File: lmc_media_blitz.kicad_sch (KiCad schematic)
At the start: 31 parts, among them J3 Conn_ARM_JTAG_SWD_10, Q1 BSS138, Q2 BSS138, U1 TPS61222DCK, U2 TLV77333PDBVR, U3 LPC804M101JDH20

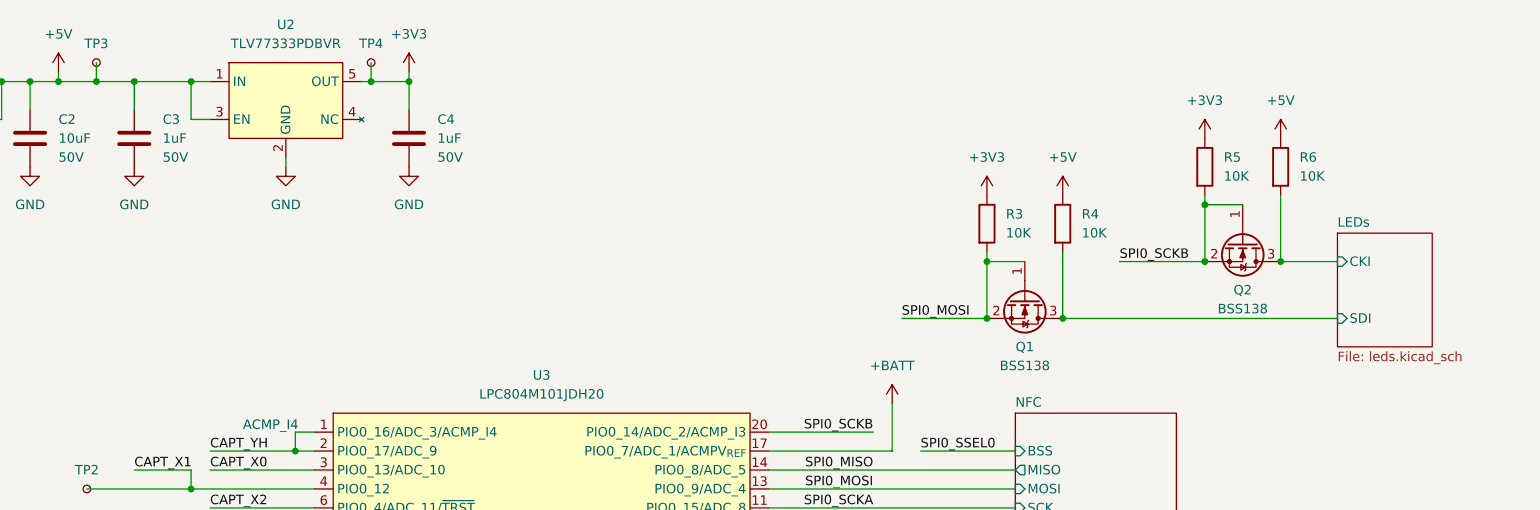
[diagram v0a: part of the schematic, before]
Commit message: Replaced n-channel FETs, LDO, and SWD connector with Basic JLCPCB parts
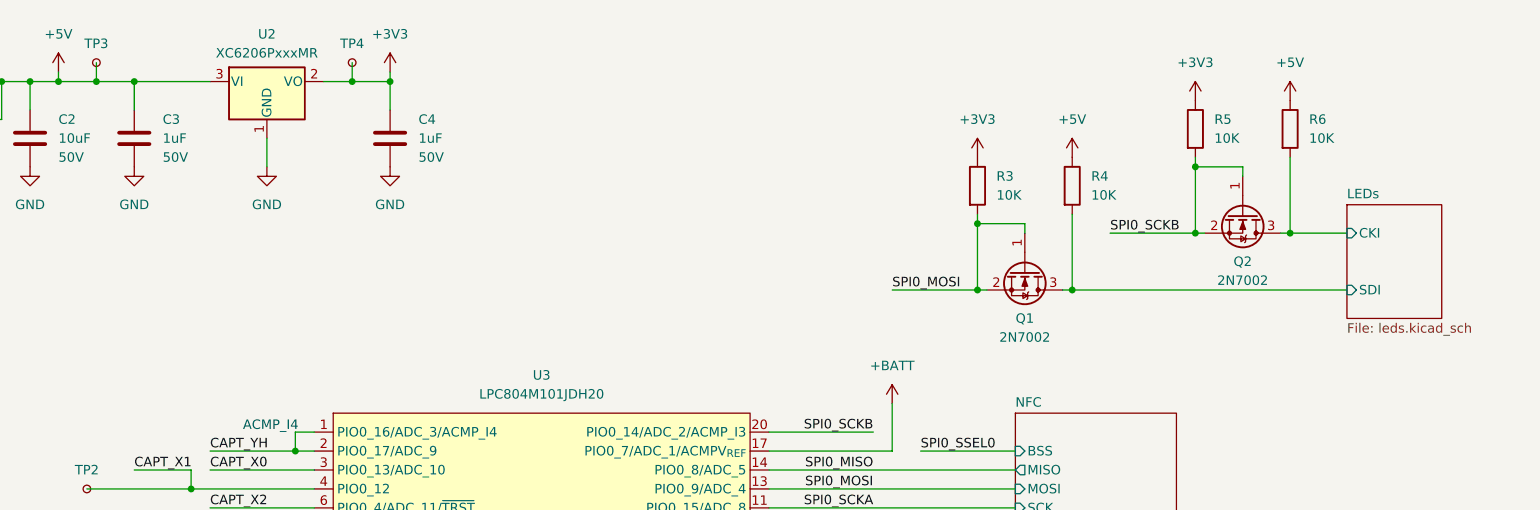
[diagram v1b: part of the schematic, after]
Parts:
- removed Q1, Q2: BSS138, Package_TO_SOT_SMD:SOT-23, symbol Transistor_FET:BSS138
- removed U2: TLV77333PDBVR, Package_TO_SOT_SMD:SOT-23-5, symbol parts:TLV77333PDBVR
- added Q1, Q2: 2N7002, Package_TO_SOT_SMD:SOT-23, symbol Transistor_FET:2N7002
- added U2: XC6206PxxxMR, Package_SO:TSSOP-20_4.4x6.5mm_P0.65mm, symbol Regulator_Linear:XC6206PxxxMR
- J3: LCSC Part # C5296739 -> C6332249; MFPN FTSH-105-01-L-DV-007-K -> HB-PH9-12725PB2GOB
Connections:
- net +3V3: now also U2.2 (VO)
- net +5V: now also U2.3 (VI)
- net GND: now also U2.1 (GND)
- net LEDs/CKI: now also Q2.3 (D)
- net LEDs/SDI: now also Q1.3 (D)
- net SPI0_MOSI: now also Q1.1 (G), Q1.2 (S)
- net SPI0_SCKB: now also Q2.1 (G), Q2.2 (S)
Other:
- moved on the sheet: C4, R3, R4, R5, R6, TP4

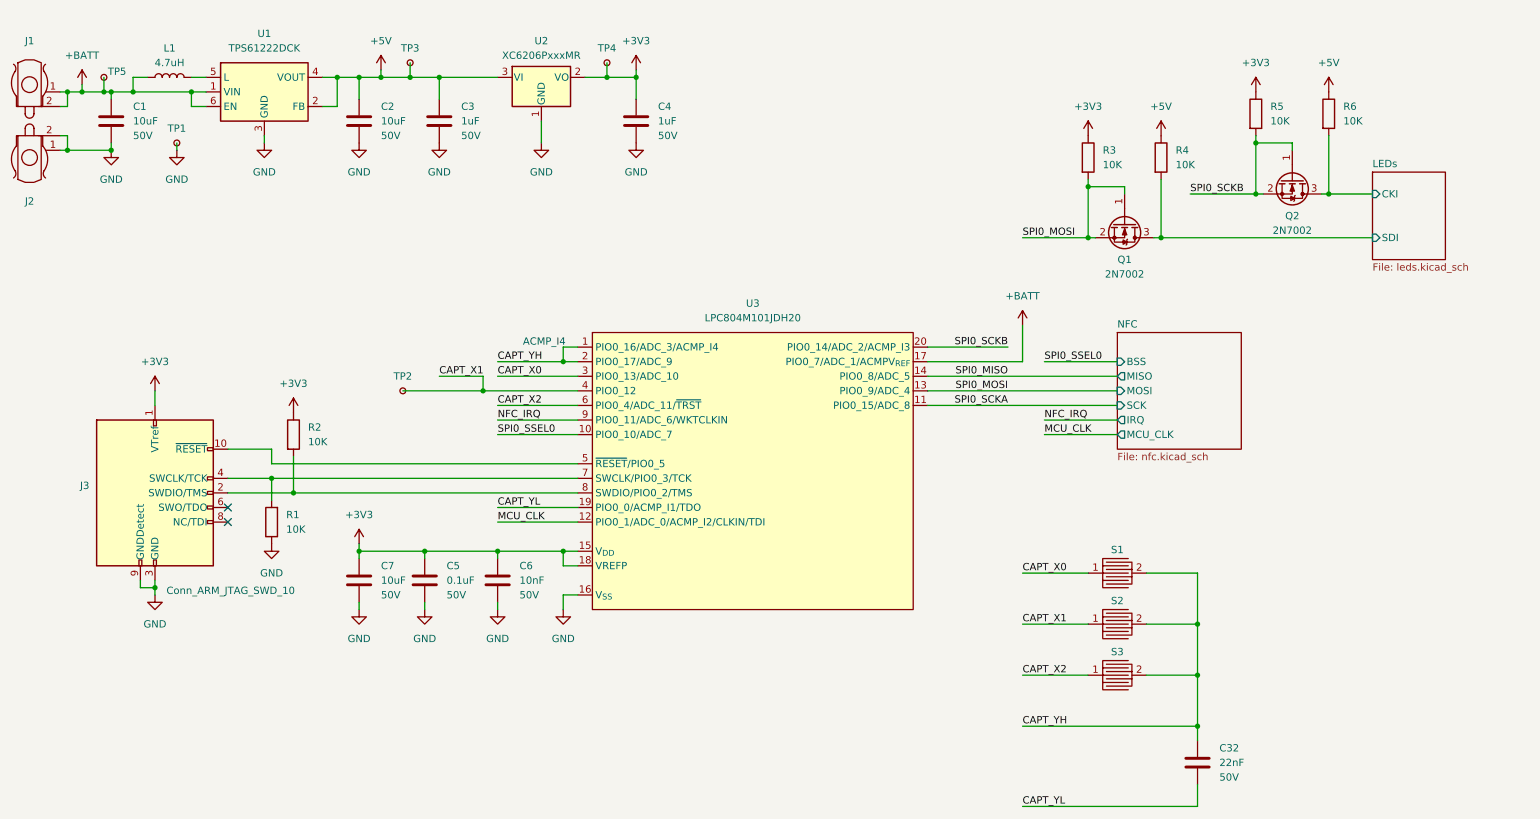
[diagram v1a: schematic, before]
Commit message: Replaced LPC TSSOP package MCU with QFN package due to unavailability.  Added separate decoupling for analog VDD rail.  Added tooling holes to board for assembly
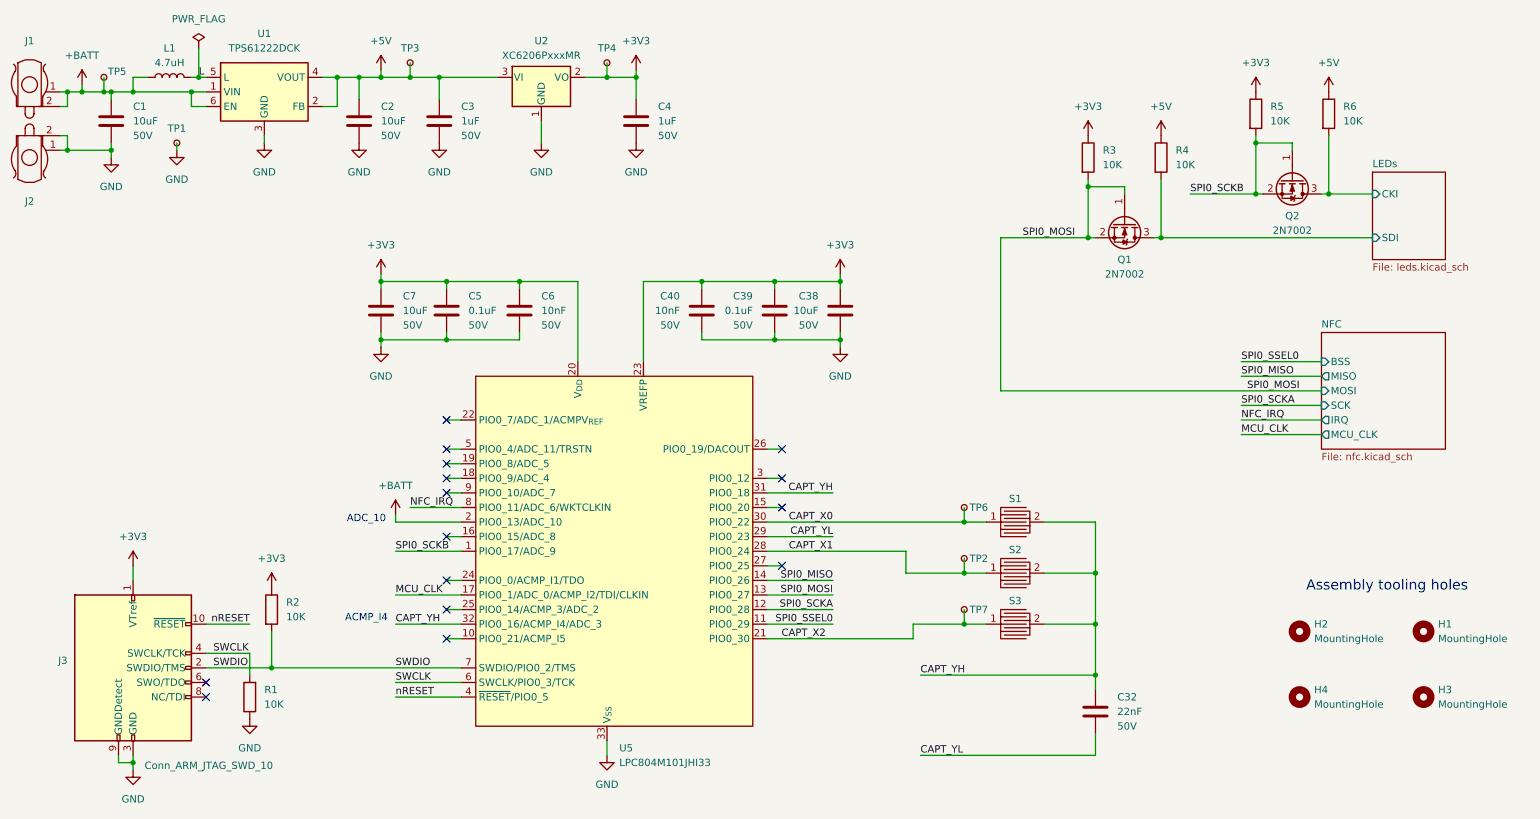
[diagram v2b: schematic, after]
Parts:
- removed U3: LPC804M101JDH20, Package_SO:TSSOP-20_4.4x6.5mm_P0.65mm, symbol parts:LPC804M101JDH20
- added C38: 10uF, Capacitor_SMD:C_0805_2012Metric, symbol Device:C
- added C39: 0.1uF, Capacitor_SMD:C_0603_1608Metric, symbol Device:C
- added C40: 10nF, Capacitor_SMD:C_0603_1608Metric, symbol Device:C
- added H1, H2, H3, H4: MountingHole, footprints:JLCPCB_ToolingHole_45.4mils, symbol Mechanical:MountingHole
- added TP6, TP7: TestPoint_Small, TestPoint:TestPoint_Pad_D2.0mm, symbol Connector:TestPoint_Small
- added U5: LPC804M101JHI33, Package_DFN_QFN:QFN-32-1EP_5x5mm_P0.5mm_EP3.7x3.7mm, symbol parts:LPC804M101JHI33
- J1, J2: LCSC Part # (none) -> C964880; MFPN (none) -> MY-AAA-02
- U2: footprint Package_SO:TSSOP-20_4.4x6.5mm_P0.65mm -> Package_TO_SOT_SMD:SOT-23-3
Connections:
- net +3V3: now also C38.2, C39.1, C40.1, U5.20 (V_{DD}), U5.23 (VREFP)
- net +BATT: now also U5.2 (PIO0_13/ADC_10)
- net CAPT_X0: now also TP6.1, U5.30 (PIO0_22)
- net CAPT_X1: now also U5.28 (PIO0_24)
- net CAPT_X2: now also TP7.1, U5.21 (PIO0_30)
- net CAPT_YH: now also U5.31 (PIO0_18), U5.32 (PIO0_16/ACMP_I4/ADC_3)
- net CAPT_YL: now also U5.29 (PIO0_23)
- net GND: now also C38.1, C39.2, C40.2, U5.33 (V_{SS})
- net MCU_CLK: now also U5.17 (PIO0_1/ADC_0/ACMP_I2/TDI/CLKIN)
- net NFC_IRQ: now also U5.8 (PIO0_11/ADC_6/WKTCLKIN)
- net SPI0_MISO: now also U5.14 (PIO0_26)
- net SPI0_MOSI: now also U5.13 (PIO0_27)
- net SPI0_SCKA: now also U5.12 (PIO0_28)
- net SPI0_SCKB: now also U5.1 (PIO0_17/ADC_9)
- net SPI0_SSEL0: now also U5.11 (PIO0_29)
- net SWDIO: now reaches J3.2 (SWDIO/TMS), R2.2
- net SWDIO: now also U5.7 (SWDIO/PIO0_2/TMS)
- net SWCLK: now reaches J3.4 (SWCLK/TCK), R1.2
- net SWCLK: now also U5.6 (SWCLK/PIO0_3/TCK)
- net L: now reaches L1.2, U1.5 (L)
- net nRESET: now reaches J3.10 (~{RESET})
- net nRESET: now also U5.4 (~{RESET}/PIO0_5)
- no-connect marks 2 -> 15
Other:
- note added: "ADC_10"
- note added: "Assembly tooling holes"
- moved on the sheet: C32, C5, C6, C7, J3, R1, R2, S1, S2, S3, TP2

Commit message: Minor cleanup.  Moved vias to let GND pours flow between islands
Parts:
- U5: MFPN (none) -> LPC804M101JHI33
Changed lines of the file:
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@@
+			)
+		)
+		(property "MFPN" "LPC804M101JHI33"
+			(at 123.19 107.95 0)
+			(effects
+				(font
+					(size 1.27 1.27)
+				)
+				(hide yes)
 			)
 		)
